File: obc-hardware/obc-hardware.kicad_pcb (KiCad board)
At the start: 2 copper layers, 90.2 x 95.9 mm, 40 parts, among them IC401 H3LIS200DLTR, IC501 ADXL335BCPZ, J301 Conn_02x26_Odd_Even, J302 Conn_02x26_Odd_Even, U201 PocketBeagle

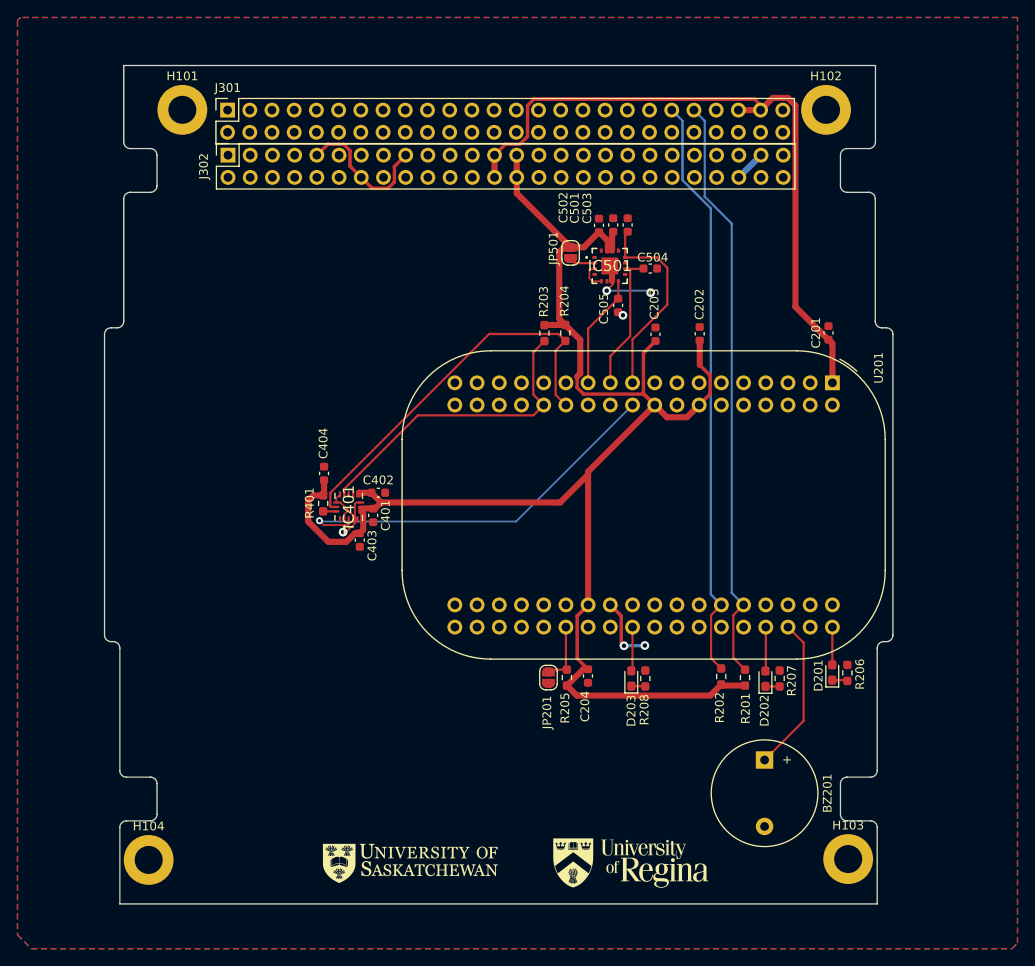
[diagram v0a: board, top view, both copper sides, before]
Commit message: added GPIO for payload
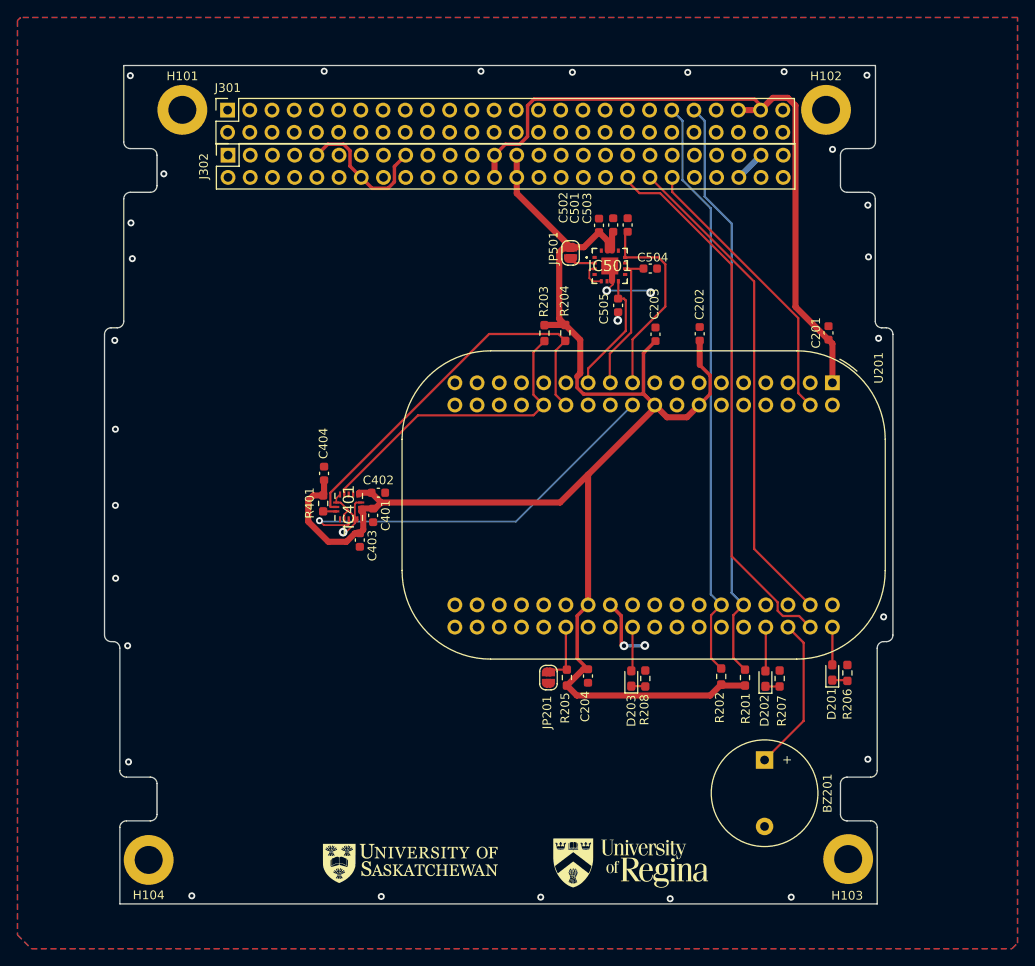
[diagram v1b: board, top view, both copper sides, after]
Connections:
- J302 pad 38: unconnected-(J302-Pin_38-Pad38) -> /CSKB/H2-38
- J302 pad 40: unconnected-(J302-Pin_40-Pad40) -> /CSKB/H2-40
- J302 pad 42: unconnected-(J302-Pin_42-Pad42) -> /CSKB/H2-42
- U201 pad 39: unconnected-(U201-GPIO23-Pad39) -> /CSKB/H2-40
- U201 pad 4: unconnected-(U201-GPIO89-Pad4) -> /CSKB/H2-42
- U201 pad 40: unconnected-(U201-GPIO58-Pad40) -> /CSKB/H2-38
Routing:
- net /CSKB/H2-38: track 0.00 -> 62.5 mm
- net /CSKB/H2-40: track 0.00 -> 56.5 mm
- net /CSKB/H2-42: track 0.00 -> 32.6 mm
- net /IMU/ZOUT: track 13.0 -> 14.2 mm
- net GND: track 51.9 -> 52.1 mm, vias 6 -> 33

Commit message: added test points
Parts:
- added REF**: OSHW-Logo2_9.8x8mm_SilkScreen, Symbol:OSHW-Logo2_9.8x8mm_SilkScreen, F.Cu at (108.8, 94.3)
- added TP101: TestPoint, TestPoint:TestPoint_THTPad_1.0x1.0mm_Drill0.5mm, F.Cu at (168.1, 115.8)
- added TP102: TestPoint, TestPoint:TestPoint_THTPad_1.0x1.0mm_Drill0.5mm, F.Cu at (144.9, 74.1)
- added TP103: TestPoint, TestPoint:TestPoint_THTPad_1.0x1.0mm_Drill0.5mm, F.Cu at (166.8, 122.4)
- added TP104: TestPoint, TestPoint:TestPoint_THTPad_1.0x1.0mm_Drill0.5mm, F.Cu at (141.7, 74.1)
- added TP105: TestPoint, TestPoint:TestPoint_THTPad_1.0x1.0mm_Drill0.5mm, F.Cu at (147.7, 74.0)
- added TP106: TestPoint, TestPoint:TestPoint_THTPad_1.0x1.0mm_Drill0.5mm, F.Cu at (132.0, 108.3)
- added TP107: TestPoint, TestPoint:TestPoint_THTPad_1.0x1.0mm_Drill0.5mm, F.Cu at (140.3, 77.7)
- added TP108: TestPoint, TestPoint:TestPoint_THTPad_1.0x1.0mm_Drill0.5mm, F.Cu at (145.0, 115.4)
- added TP109: TestPoint, TestPoint:TestPoint_THTPad_1.0x1.0mm_Drill0.5mm, F.Cu at (133.0, 84.2)
- added TP110: TestPoint, TestPoint:TestPoint_THTPad_1.0x1.0mm_Drill0.5mm, F.Cu at (132.9, 80.7)
- added TP111: TestPoint, TestPoint:TestPoint_THTPad_1.0x1.0mm_Drill0.5mm, F.Cu at (165.8, 115.9)
- added TP112: TestPoint, TestPoint:TestPoint_THTPad_1.0x1.0mm_Drill0.5mm, F.Cu at (132.1, 105.9)
- moved G*** 45.1 mm to (123.4, 124.2)
- moved G*** 10.3 mm to (127.2, 130.9)
- moved G*** 6.84 mm to (157.6, 131.0)
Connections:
- U201 pad 24: unconnected-(U201-VOUT-Pad24) -> /Pocket Beagle/VOUT-24
- U201 pad 25: unconnected-(U201-AIN3(1.8V)-Pad25) -> /Pocket Beagle/AIN3
- U201 pad 27: unconnected-(U201-AIN4(1.8V)-Pad27) -> /Pocket Beagle/AIN4
- U201 pad 33: unconnected-(U201-PRU0.1-Pad33) -> /Pocket Beagle/PRU0.1
- U201 pad 34: unconnected-(U201-GPIO26-Pad34) -> /Pocket Beagle/GPIO26
- U201 pad 36: unconnected-(U201-PWM0A-Pad36) -> /Pocket Beagle/PWM0A
- U201 pad 49: unconnected-(U201-VOUT-Pad49) -> /Pocket Beagle/VOUT-49
- U201 pad 50: unconnected-(U201-BAT.VIN-Pad50) -> /Pocket Beagle/BAT.VIN
- U201 pad 55: unconnected-(U201-GPIO27-Pad55) -> /Pocket Beagle/GPIO27
- U201 pad 68: unconnected-(U201-PRU0.2-Pad68) -> /Pocket Beagle/PRU0.2
- U201 pad 69: unconnected-(U201-GPIO45-Pad69) -> /Pocket Beagle/GPIO45
- U201 pad 71: unconnected-(U201-AIN5(3.3V)-Pad71) -> /Pocket Beagle/AIN5
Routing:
- net /Pocket Beagle/VOUT-24: track 0.00 -> 16.2 mm
- net /Pocket Beagle/VOUT-49: track 0.00 -> 15.2 mm
- net /Pocket Beagle/AIN4: track 0.00 -> 12.2 mm
- net /Pocket Beagle/GPIO26: track 0.00 -> 11.7 mm
- net /Pocket Beagle/GPIO45: track 0.00 -> 11.6 mm
- net /Pocket Beagle/AIN3: track 0.00 -> 10.6 mm
- net /Pocket Beagle/GPIO27: track 0.00 -> 10.2 mm
- net /Pocket Beagle/AIN5: track 0.00 -> 8.89 mm
- net /Pocket Beagle/PWM0A: track 0.00 -> 7.64 mm
- net /Pocket Beagle/PRU0.1: track 0.00 -> 5.73 mm
- net /Pocket Beagle/BAT.VIN: track 0.00 -> 5.50 mm
- net /Pocket Beagle/PRU0.2: track 0.00 -> 5.19 mm
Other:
- board text added: "github.com/SkCubeSat/obc-hardware"
